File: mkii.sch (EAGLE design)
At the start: 52 parts, among them IC1 ATMEGA32U4, Q1 16MHz, U1 GTL2003, U2 TS1117, U3 PRTR5V0U2AX, X1 MINI-USB-32005-301

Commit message: growing sheep
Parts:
- U$4: value SCHAF5MM -> SCHAF7MM; device grafiken:SCHAF5MM -> grafiken:SCHAF7MM
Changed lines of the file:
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@@
 <grid distance="0.1" unitdist="inch" unit="mm" style="lines" multiple="1" display="yes" altdistance="0.01" altunitdist="inch" altunit="mm"/>
 <layers>
-<layer number="1" name="Top" color="4" fill="1" visible="no" active="no"/>
-<layer number="2" name="Route2" color="1" fill="3" visible="no" active="no"/>
-<layer number="3" name="Route3" color="4" fill="3" visible="no" active="no"/>
-<layer number="4" name="Route4" color="1" fill="4" visible="no" active="no"/>
-<layer number="5" name="Route5" color="4" fill="4" visible="no" active="no"/>
-<layer number="6" name="Route6" color="1" fill="8" visible="no" active="no"/>
-<layer number="7" name="Route7" color="4" fill="8" visible="no" active="no"/>
-<layer number="8" name="Route8" color="1" fill="2" visible="no" active="no"/>
-<layer number="9" name="Route9" color="4" fill="2" visible="no" active="no"/>
-<layer number="10" name="Route10" color="1" fill="7" visible="no" active="no"/>
-<layer number="11" name="Route11" color="4" fill="7" visible="no" active="no"/>
-<layer number="12" name="Route12" color="1" fill="5" visible="no" active="no"/>
-<layer number="13" name="Route13" color="4" fill="5" visible="no" active="no"/>
-<layer number="14" name="Route14" color="1" fill="6" visible="no" active="no"/>
-<layer number="15" name="Route15" color="4" fill="6" visible="no" active="no"/>
-<layer number="16" name="Bottom" color="1" fill="1" visible="no" active="no"/>
-<layer number="17" name="Pads" color="2" fill="1" visible="no" active="no"/>
-<layer number="18" name="Vias" color="2" fill="1" visible="no" active="no"/>
-<layer number="19" name="Unrouted" color="6" fill="1" visible="no" active="no"/>
-<layer number="20" name="Dimension" color="15" fill="1" visible="no" active="no"/>
-<layer number="21" name="tPlace" color="7" fill="1" visible="no" active="no"/>
-<layer number="22" name="bPlace" color="7" fill="1" visible="no" active="no"/>
-<layer number="23" name="tOrigins" color="15" fill="1" visible="no" active="no"/>
-<layer number="24" name="bOrigins" color="15" fill="1" visible="no" active="no"/>
-<layer number="25" name="tNames" color="7" fill="1" visible="no" active="no"/>
-<layer number="26" name="bNames" color="7" fill="1" visible="no" active="no"/>
-<layer number="27" name="tValues" color="7" fill="1" visible="no" active="no"/>
-<layer number="28" name="bValues" color="7" fill="1" visible="no" active="no"/>
+<layer number="1" name="Top" color="4" fill="1" visible="yes" active="no"/>
+<layer number="2" name="Route2" color="1" fill="3" visible="yes" active="no"/>
+<layer number="3" name="Route3" color="4" fill="3" visible="yes" active="no"/>
+<layer number="4" name="Route4" color="1" fill="4" visible="yes" active="no"/>
+<layer number="5" name="Route5" color="4" fill="4" visible="yes" active="no"/>
+<layer number="6" name="Route6" color="1" fill="8" visible="yes" active="no"/>
+<layer number="7" name="Route7" color="4" fill="8" visible="yes" active="no"/>
+<layer number="8" name="Route8" color="1" fill="2" visible="yes" active="no"/>
+<layer number="9" name="Route9" color="4" fill="2" visible="yes" active="no"/>
+<layer number="10" name="Route10" color="1" fill="7" visible="yes" active="no"/>
+<layer number="11" name="Route11" color="4" fill="7" visible="yes" active="no"/>
+<layer number="12" name="Route12" color="1" fill="5" visible="yes" active="no"/>
+<layer number="13" name="Route13" color="4" fill="5" visible="yes" active="no"/>
+<layer number="14" name="Route14" color="1" fill="6" visible="yes" active="no"/>
+<layer number="15" name="Route15" color="4" fill="6" visible="yes" active="no"/>
+<layer number="16" name="Bottom" color="1" fill="1" visible="yes" active="no"/>
+<layer number="17" name="Pads" color="2" fill="1" visible="yes" active="no"/>
+<layer number="18" name="Vias" color="2" fill="1" visible="yes" active="no"/>
+<layer number="19" name="Unrouted" color="6" fill="1" visible="yes" active="no"/>
+<layer number="20" name="Dimension" color="15" fill="1" visible="yes" active="no"/>
+<layer number="21" name="tPlace" color="7" fill="1" visible="yes" active="no"/>
+<layer number="22" name="bPlace" color="7" fill="1" visible="yes" active="no"/>
+<layer number="23" name="tOrigins" color="15" fill="1" visible="yes" active="no"/>
+<layer number="24" name="bOrigins" color="15" fill="1" visible="yes" active="no"/>
+<layer number="25" name="tNames" color="7" fill="1" visible="yes" active="no"/>
+<layer number="26" name="bNames" color="7" fill="1" visible="yes" active="no"/>
+<layer number="27" name="tValues" color="7" fill="1" visible="yes" active="no"/>
+<layer number="28" name="bValues" color="7" fill="1" visible="yes" active="no"/>
 <layer number="29" name="tStop" color="7" fill="3" visible="no" active="no"/>
 <layer number="30" name="bStop" color="7" fill="6" visible="no" active="no"/>
@@
 <layer number="35" name="tGlue" color="7" fill="4" visible="no" active="no"/>
 <layer number="36" name="bGlue" color="7" fill="5" visible="no" active="no"/>
-<layer number="37" name="tTest" color="7" fill="1" visible="no" active="no"/>
-<layer number="38" name="bTest" color="7" fill="1" visible="no" active="no"/>
+<layer number="37" name="tTest" color="7" fill="1" visible="yes" active="no"/>
+<layer number="38" name="bTest" color="7" fill="1" visible="yes" active="no"/>
 <layer number="39" name="tKeepout" color="4" fill="11" visible="no" active="no"/>
 <layer number="40" name="bKeepout" color="1" fill="11" visible="no" active="no"/>
@@
 <layer number="44" name="Drills" color="7" fill="1" visible="no" active="no"/>
 <layer number="45" name="Holes" color="7" fill="1" visible="no" active="no"/>
-<layer number="46" name="Milling" color="3" fill="1" visible="no" active="no"/>
-<layer number="47" name="Measures" color="7" fill="1" visible="no" active="no"/>
-<layer number="48" name="Document" color="7" fill="1" visible="no" active="no"/>
-<layer number="49" name="Reference" color="7" fill="1" visible="no" active="no"/>
-<layer number="50" name="dxf" color="7" fill="1" visible="no" active="no"/>
-<layer number="51" name="tDocu" color="7" fill="1" visible="no" active="no"/>
-<layer number="52" name="bDocu" color="7" fill="1" visible="no" active="no"/>
-<layer number="53" name="tPadExt" color="7" fill="1" visible="no" active="no"/>
-<layer number="54" name="bPadExt" color="1" fill="1" visible="no" active="no"/>
-<layer number="56" name="wert" color="7" fill="1" visible="no" active="no"/>
-<layer number="57" name="tCAD" color="7" fill="1" visible="no" active="no"/>
+<layer number="46" name="Milling" color="3" fill="1" visible="yes" active="no"/>
+<layer number="47" name="Measures" color="7" fill="1" visible="yes" active="no"/>
+<layer number="48" name="Document" color="7" fill="1" visible="yes" active="no"/>
+<layer number="49" name="Reference" color="7" fill="1" visible="yes" active="no"/>
+<layer number="50" name="dxf" color="7" fill="1" visible="yes" active="no"/>
+<layer number="51" name="tDocu" color="7" fill="1" visible="yes" active="no"/>
+<layer number="52" name="bDocu" color="7" fill="1" visible="yes" active="no"/>
+<layer number="53" name="tPadExt" color="7" fill="1" visible="yes" active="no"/>
+<layer number="54" name="bPadExt" color="1" fill="1" visible="yes" active="no"/>
+<layer number="56" name="wert" color="7" fill="1" visible="yes" active="no"/>
+<layer number="57" name="tCAD" color="7" fill="1" visible="yes" active="no"/>
 <layer number="91" name="Nets" color="2" fill="1" visible="yes" active="yes"/>
 <layer number="92" name="Busses" color="1" fill="1" visible="yes" active="yes"/>
@@
 <part name="U$2" library="creative-commons" deviceset="BY" device="-TPLACE-HS"/>
 <part name="U$3" library="creative-commons" deviceset="SA" device="-TPLACE-HALF"/>
-<part name="U$4" library="grafiken" deviceset="SCHAF" device="5MM" value="SCHAF5MM"/>
+<part name="U$4" library="grafiken" deviceset="SCHAF" device="7MM" value="SCHAF7MM"/>
 <part name="U$5" library="grafiken" deviceset="PM-CHERRY" device="5"/>
 <part name="U$6" library="grafiken" deviceset="PM-PILL" device="5"/>

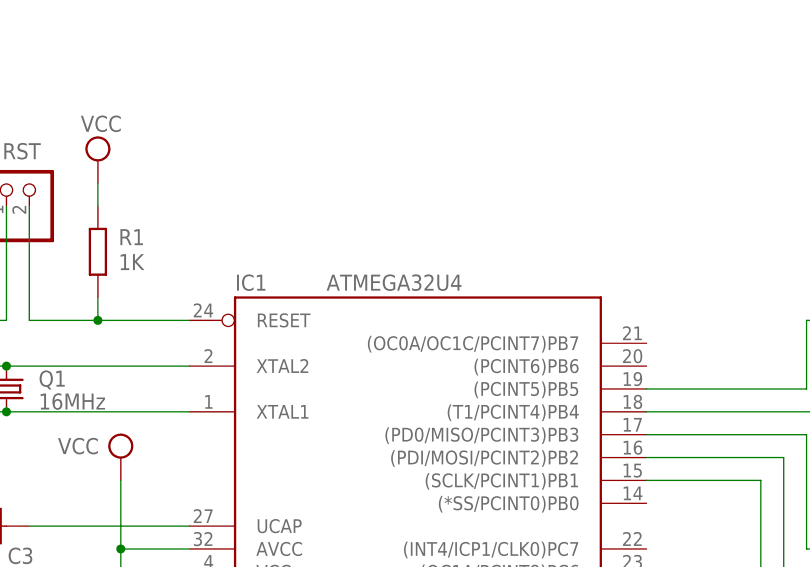
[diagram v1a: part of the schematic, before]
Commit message: atmega32u2, not u4
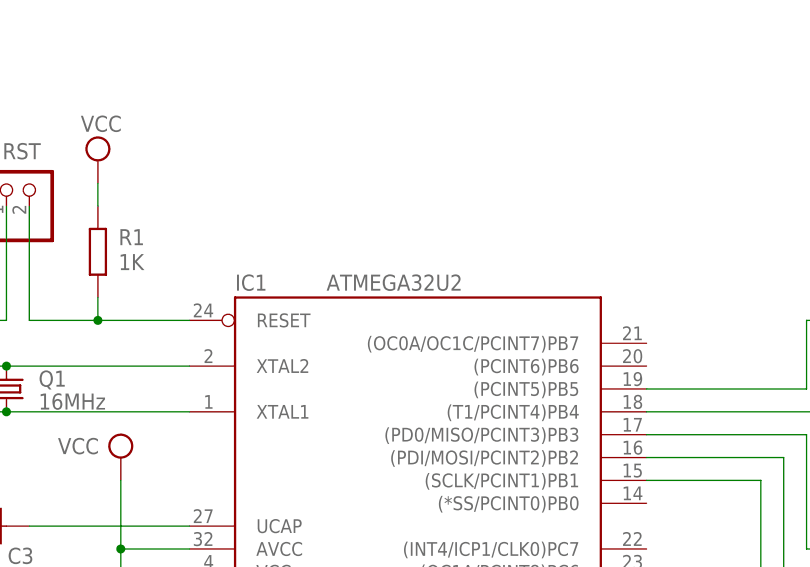
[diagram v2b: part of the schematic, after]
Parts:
- IC1: value ATMEGA32U4 -> ATMEGA32U2
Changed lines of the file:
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@@
 <grid distance="0.1" unitdist="inch" unit="mm" style="lines" multiple="1" display="yes" altdistance="0.01" altunitdist="inch" altunit="mm"/>
 <layers>
-<layer number="1" name="Top" color="4" fill="1" visible="yes" active="no"/>
-<layer number="2" name="Route2" color="1" fill="3" visible="yes" active="no"/>
-<layer number="3" name="Route3" color="4" fill="3" visible="yes" active="no"/>
-<layer number="4" name="Route4" color="1" fill="4" visible="yes" active="no"/>
-<layer number="5" name="Route5" color="4" fill="4" visible="yes" active="no"/>
-<layer number="6" name="Route6" color="1" fill="8" visible="yes" active="no"/>
-<layer number="7" name="Route7" color="4" fill="8" visible="yes" active="no"/>
-<layer number="8" name="Route8" color="1" fill="2" visible="yes" active="no"/>
-<layer number="9" name="Route9" color="4" fill="2" visible="yes" active="no"/>
-<layer number="10" name="Route10" color="1" fill="7" visible="yes" active="no"/>
-<layer number="11" name="Route11" color="4" fill="7" visible="yes" active="no"/>
-<layer number="12" name="Route12" color="1" fill="5" visible="yes" active="no"/>
-<layer number="13" name="Route13" color="4" fill="5" visible="yes" active="no"/>
-<layer number="14" name="Route14" color="1" fill="6" visible="yes" active="no"/>
-<layer number="15" name="Route15" color="4" fill="6" visible="yes" active="no"/>
-<layer number="16" name="Bottom" color="1" fill="1" visible="yes" active="no"/>
-<layer number="17" name="Pads" color="2" fill="1" visible="yes" active="no"/>
-<layer number="18" name="Vias" color="2" fill="1" visible="yes" active="no"/>
-<layer number="19" name="Unrouted" color="6" fill="1" visible="yes" active="no"/>
-<layer number="20" name="Dimension" color="15" fill="1" visible="yes" active="no"/>
-<layer number="21" name="tPlace" color="7" fill="1" visible="yes" active="no"/>
-<layer number="22" name="bPlace" color="7" fill="1" visible="yes" active="no"/>
-<layer number="23" name="tOrigins" color="15" fill="1" visible="yes" active="no"/>
-<layer number="24" name="bOrigins" color="15" fill="1" visible="yes" active="no"/>
-<layer number="25" name="tNames" color="7" fill="1" visible="yes" active="no"/>
-<layer number="26" name="bNames" color="7" fill="1" visible="yes" active="no"/>
-<layer number="27" name="tValues" color="7" fill="1" visible="yes" active="no"/>
-<layer number="28" name="bValues" color="7" fill="1" visible="yes" active="no"/>
+<layer number="1" name="Top" color="4" fill="1" visible="no" active="no"/>
+<layer number="2" name="Route2" color="1" fill="3" visible="no" active="no"/>
+<layer number="3" name="Route3" color="4" fill="3" visible="no" active="no"/>
+<layer number="4" name="Route4" color="1" fill="4" visible="no" active="no"/>
+<layer number="5" name="Route5" color="4" fill="4" visible="no" active="no"/>
+<layer number="6" name="Route6" color="1" fill="8" visible="no" active="no"/>
+<layer number="7" name="Route7" color="4" fill="8" visible="no" active="no"/>
+<layer number="8" name="Route8" color="1" fill="2" visible="no" active="no"/>
+<layer number="9" name="Route9" color="4" fill="2" visible="no" active="no"/>
+<layer number="10" name="Route10" color="1" fill="7" visible="no" active="no"/>
+<layer number="11" name="Route11" color="4" fill="7" visible="no" active="no"/>
+<layer number="12" name="Route12" color="1" fill="5" visible="no" active="no"/>
+<layer number="13" name="Route13" color="4" fill="5" visible="no" active="no"/>
+<layer number="14" name="Route14" color="1" fill="6" visible="no" active="no"/>
+<layer number="15" name="Route15" color="4" fill="6" visible="no" active="no"/>
+<layer number="16" name="Bottom" color="1" fill="1" visible="no" active="no"/>
+<layer number="17" name="Pads" color="2" fill="1" visible="no" active="no"/>
+<layer number="18" name="Vias" color="2" fill="1" visible="no" active="no"/>
+<layer number="19" name="Unrouted" color="6" fill="1" visible="no" active="no"/>
+<layer number="20" name="Dimension" color="15" fill="1" visible="no" active="no"/>
+<layer number="21" name="tPlace" color="7" fill="1" visible="no" active="no"/>
+<layer number="22" name="bPlace" color="7" fill="1" visible="no" active="no"/>
+<layer number="23" name="tOrigins" color="15" fill="1" visible="no" active="no"/>
+<layer number="24" name="bOrigins" color="15" fill="1" visible="no" active="no"/>
+<layer number="25" name="tNames" color="7" fill="1" visible="no" active="no"/>
+<layer number="26" name="bNames" color="7" fill="1" visible="no" active="no"/>
+<layer number="27" name="tValues" color="7" fill="1" visible="no" active="no"/>
+<layer number="28" name="bValues" color="7" fill="1" visible="no" active="no"/>
 <layer number="29" name="tStop" color="7" fill="3" visible="no" active="no"/>
 <layer number="30" name="bStop" color="7" fill="6" visible="no" active="no"/>
@@
 <layer number="35" name="tGlue" color="7" fill="4" visible="no" active="no"/>
 <layer number="36" name="bGlue" color="7" fill="5" visible="no" active="no"/>
-<layer number="37" name="tTest" color="7" fill="1" visible="yes" active="no"/>
-<layer number="38" name="bTest" color="7" fill="1" visible="yes" active="no"/>
+<layer number="37" name="tTest" color="7" fill="1" visible="no" active="no"/>
+<layer number="38" name="bTest" color="7" fill="1" visible="no" active="no"/>
 <layer number="39" name="tKeepout" color="4" fill="11" visible="no" active="no"/>
 <layer number="40" name="bKeepout" color="1" fill="11" visible="no" active="no"/>
@@
 <layer number="44" name="Drills" color="7" fill="1" visible="no" active="no"/>
 <layer number="45" name="Holes" color="7" fill="1" visible="no" active="no"/>
-<layer number="46" name="Milling" color="3" fill="1" visible="yes" active="no"/>
-<layer number="47" name="Measures" color="7" fill="1" visible="yes" active="no"/>
-<layer number="48" name="Document" color="7" fill="1" visible="yes" active="no"/>
-<layer number="49" name="Reference" color="7" fill="1" visible="yes" active="no"/>
-<layer number="50" name="dxf" color="7" fill="1" visible="yes" active="no"/>
-<layer number="51" name="tDocu" color="7" fill="1" visible="yes" active="no"/>
-<layer number="52" name="bDocu" color="7" fill="1" visible="yes" active="no"/>
-<layer number="53" name="tPadExt" color="7" fill="1" visible="yes" active="no"/>
-<layer number="54" name="bPadExt" color="1" fill="1" visible="yes" active="no"/>
-<layer number="56" name="wert" color="7" fill="1" visible="yes" active="no"/>
-<layer number="57" name="tCAD" color="7" fill="1" visible="yes" active="no"/>
+<layer number="46" name="Milling" color="3" fill="1" visible="no" active="no"/>
+<layer number="47" name="Measures" color="7" fill="1" visible="no" active="no"/>
+<layer number="48" name="Document" color="7" fill="1" visible="no" active="no"/>
+<layer number="49" name="Reference" color="7" fill="1" visible="no" active="no"/>
+<layer number="50" name="dxf" color="7" fill="1" visible="no" active="no"/>
+<layer number="51" name="tDocu" color="7" fill="1" visible="no" active="no"/>
+<layer number="52" name="bDocu" color="7" fill="1" visible="no" active="no"/>
+<layer number="53" name="tPadExt" color="7" fill="1" visible="no" active="no"/>
+<layer number="54" name="bPadExt" color="1" fill="1" visible="no" active="no"/>
+<layer number="56" name="wert" color="7" fill="1" visible="no" active="no"/>
+<layer number="57" name="tCAD" color="7" fill="1" visible="no" active="no"/>
 <layer number="91" name="Nets" color="2" fill="1" visible="yes" active="yes"/>
 <layer number="92" name="Busses" color="1" fill="1" visible="yes" active="yes"/>
@@
 </classes>
 <parts>
-<part name="IC1" library="at90usb" deviceset="AT90USB162-*" device="AU" value="ATMEGA32U4"/>
+<part name="IC1" library="at90usb" deviceset="AT90USB162-*" device="AU" value="ATMEGA32U2"/>
 <part name="SUPPLY1" library="supply2" deviceset="GND" device=""/>
 <part name="SUPPLY3" library="supply2" deviceset="VCC" device=""/>

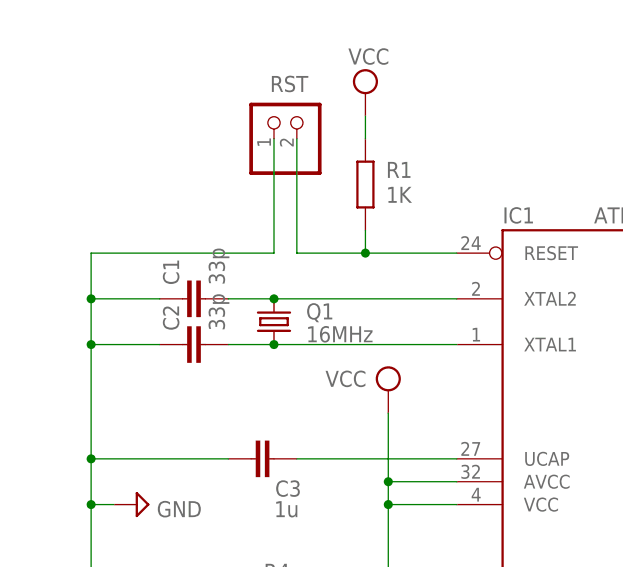
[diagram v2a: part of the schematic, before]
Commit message: 22p cap for crystal
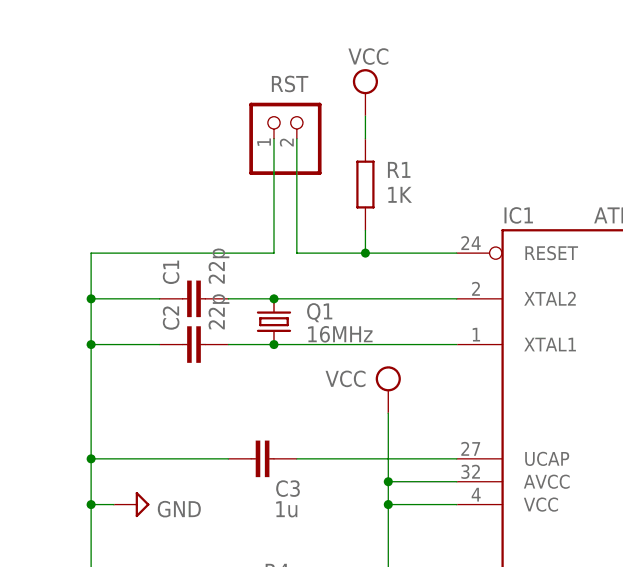
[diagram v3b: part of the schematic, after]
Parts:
- C1, C2: value 33p -> 22p
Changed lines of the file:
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@@
 <part name="SUPPLY2" library="supply2" deviceset="V+" device=""/>
 <part name="Q1" library="crystal" deviceset="CRYSTAL" device="HC49S" value="16MHz"/>
-<part name="C1" library="rcl" deviceset="C-EU" device="C0603" value="33p"/>
-<part name="C2" library="rcl" deviceset="C-EU" device="C0603" value="33p"/>
+<part name="C1" library="rcl" deviceset="C-EU" device="C0603" value="22p"/>
+<part name="C2" library="rcl" deviceset="C-EU" device="C0603" value="22p"/>
 <part name="SUPPLY4" library="supply2" deviceset="GND" device=""/>
 <part name="R1" library="rcl" deviceset="R-EU_" device="R0603" value="1K"/>
